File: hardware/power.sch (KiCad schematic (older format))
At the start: 14 parts, among them P201 CONN_02X05, U201 MP1469

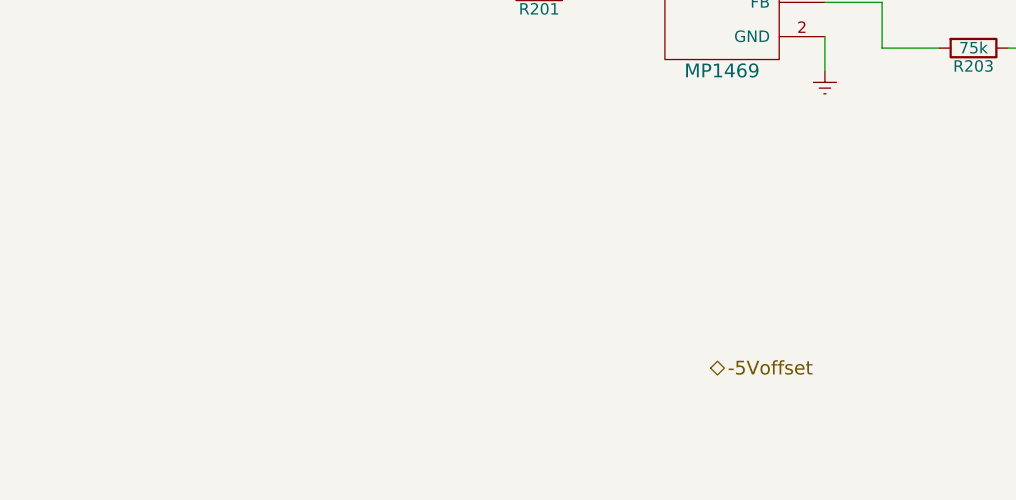
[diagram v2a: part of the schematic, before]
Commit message: updated footprint & first tracks laid
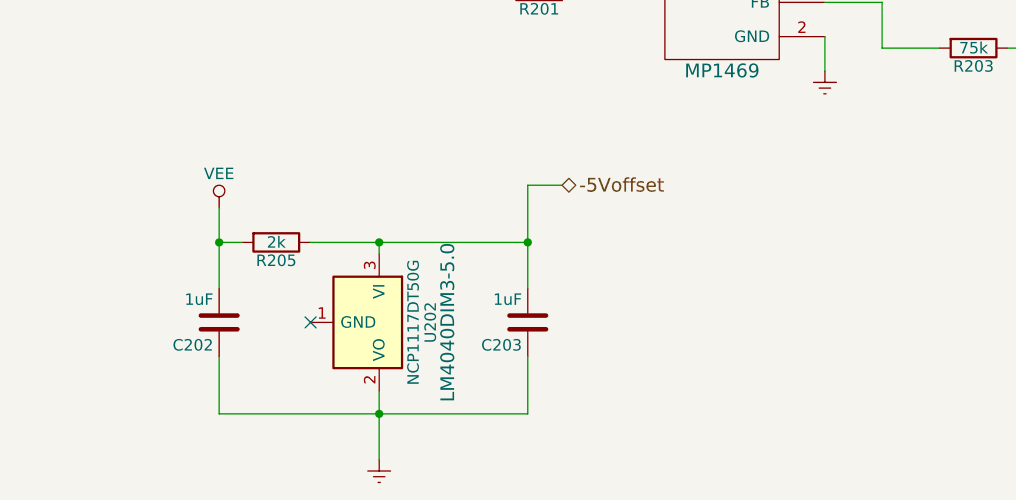
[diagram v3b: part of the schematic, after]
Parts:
- added C202, C203: 1uF, Capacitors_SMD:C_0805_HandSoldering, symbol C
- added R205: 2k, Resistors_SMD:R_0805_HandSoldering, symbol R
- added U202: NCP1117DT50G, TO_SOT_Packages_SMD:SOT-23, symbol NCP1117DT50G
- C201: footprint Capacitors_THT:C_Rect_L11.5mm_W2.8mm_P10.00mm_MKT -> Capacitors_SMD:C_0805_HandSoldering
- C244: footprint Capacitors_THT:C_Axial_L5.1mm_D3.1mm_P7.50mm_Horizontal -> Capacitors_SMD:C_0805_HandSoldering
- CP201, CP202, CP203: footprint Capacitors_THT:CP_Radial_D10.0mm_P5.00mm -> Capacitors_THT:CP_Radial_D5.0mm_P2.00mm
- R201, R202, R203, R204: footprint Resistors_Universal:Resistor_SMD+THTuniversal_0805to1206_RM10_HandSoldering_RevA_Date25Jun2010 -> Resistors_SMD:R_0805_HandSoldering
- U201: footprint (none) -> TO_SOT_Packages_SMD:SOT-23-6
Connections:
- net -5Voffset: now also C203.2, R205.1, U202.3 (VI)
- net Earth: now also C202.1, C203.1, U202.2 (VO)
- net VEE: now also C202.2, R205.2
- no-connect marks 0 -> 1
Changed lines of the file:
@@
 F 0 "CP201" H 4975 2350 50  0000 L CNN
 F 1 "22uF" H 4975 2150 50  0000 L CNN
-F 2 "Capacitors_THT:CP_Radial_D10.0mm_P5.00mm" H 4988 2100 50  0001 C CNN
+F 2 "Capacitors_THT:CP_Radial_D5.0mm_P2.00mm" H 4988 2100 50  0001 C CNN
 F 3 "" H 4950 2250 50  0000 C CNN
 	1    4950 2250
@@
 F 0 "CP202" H 4975 2850 50  0000 L CNN
 F 1 "22uF" H 4975 2650 50  0000 L CNN
-F 2 "Capacitors_THT:CP_Radial_D10.0mm_P5.00mm" H 4988 2600 50  0001 C CNN
+F 2 "Capacitors_THT:CP_Radial_D5.0mm_P2.00mm" H 4988 2600 50  0001 C CNN
 F 3 "" H 4950 2750 50  0000 C CNN
 	1    4950 2750
@@
 F 0 "R201" V 5530 3250 50  0000 C CNN
 F 1 "100k" V 5450 3250 50  0000 C CNN
-F 2 "Resistors_Universal:Resistor_SMD+THTuniversal_0805to1206_RM10_HandSoldering_RevA_Date25Jun2010" V 5380 3250 50  0001 C CNN
+F 2 "Resistors_SMD:R_0805_HandSoldering" V 5380 3250 50  0001 C CNN
 F 3 "" H 5450 3250 50  0000 C CNN
 	1    5450 3250
@@
 F 0 "U201" H 6250 3650 60  0000 C CNN
 F 1 "MP1469" H 6250 2900 60  0000 C CNN
-F 2 "" H 6100 3150 60  0001 C CNN
+F 2 "TO_SOT_Packages_SMD:SOT-23-6" H 6100 3150 60  0001 C CNN
 F 3 "" H 6100 3150 60  0001 C CNN
 	1    6250 3250
@@
 F 0 "C201" V 6900 3050 50  0000 L CNN
 F 1 "1uF" V 7000 3050 50  0000 L CNN
-F 2 "Capacitors_THT:C_Rect_L11.5mm_W2.8mm_P10.00mm_MKT" H 6988 2850 50  0001 C CNN
+F 2 "Capacitors_SMD:C_0805_HandSoldering" H 6988 2850 50  0001 C CNN
 F 3 "" H 6950 3000 50  0000 C CNN
 	1    6950 3000
@@
 F 0 "R203" V 7430 3500 50  0000 C CNN
 F 1 "75k" V 7350 3500 50  0000 C CNN
-F 2 "Resistors_Universal:Resistor_SMD+THTuniversal_0805to1206_RM10_HandSoldering_RevA_Date25Jun2010" V 7280 3500 50  0001 C CNN
+F 2 "Resistors_SMD:R_0805_HandSoldering" V 7280 3500 50  0001 C CNN
 F 3 "" H 7350 3500 50  0000 C CNN
 	1    7350 3500
@@
 F 0 "CP203" H 8225 3400 50  0000 L CNN
 F 1 "22uF" H 8225 3200 50  0000 L CNN
-F 2 "Capacitors_THT:CP_Radial_D10.0mm_P5.00mm" H 8238 3150 50  0001 C CNN
+F 2 "Capacitors_THT:CP_Radial_D5.0mm_P2.00mm" H 8238 3150 50  0001 C CNN
 F 3 "" H 8200 3300 50  0000 C CNN
 	1    8200 3300
@@
 F 0 "R204" V 7880 3700 50  0000 C CNN
 F 1 "7k68" V 7800 3700 50  0000 C CNN
-F 2 "Resistors_Universal:Resistor_SMD+THTuniversal_0805to1206_RM10_HandSoldering_RevA_Date25Jun2010" V 7730 3700 50  0001 C CNN
+F 2 "Resistors_SMD:R_0805_HandSoldering" V 7730 3700 50  0001 C CNN
 F 3 "" H 7800 3700 50  0000 C CNN
 	1    7800 3700
@@
 F 0 "R202" V 7880 3300 50  0000 C CNN
 F 1 "402k2" V 7800 3300 50  0000 C CNN
-F 2 "Resistors_Universal:Resistor_SMD+THTuniversal_0805to1206_RM10_HandSoldering_RevA_Date25Jun2010" V 7730 3300 50  0001 C CNN
+F 2 "Resistors_SMD:R_0805_HandSoldering" V 7730 3300 50  0001 C CNN
 F 3 "" H 7800 3300 50  0000 C CNN
 	1    7800 3300
@@
 F 0 "C244" H 8625 3400 50  0000 L CNN
 F 1 "100nF" H 8625 3200 50  0000 L CNN
-F 2 "Capacitors_THT:C_Axial_L5.1mm_D3.1mm_P7.50mm_Horizontal" H 8638 3150 50  0001 C CNN
+F 2 "Capacitors_SMD:C_0805_HandSoldering" H 8638 3150 50  0001 C CNN
 F 3 "" H 8600 3300 50  0000 C CNN
 	1    8600 3300
@@
 Wire Wire Line
 	6650 1100 6650 1300
-Text HLabel 6200 4900 2    60   BiDi ~ 0
+Text HLabel 5550 4100 2    60   BiDi ~ 0
 -5Voffset
 $Comp
@@
 Wire Wire Line
 	7600 1300 7600 1100
+$Comp
+L NCP1117DT50G U202
+U 1 1 5BE9A6E8
+P 4750 4700
+F 0 "U202" H 4750 4925 50  0000 C CNN
+F 1 "NCP1117DT50G" H 4750 4850 50  0000 C CNN
+F 2 "TO_SOT_Packages_SMD:SOT-23" H 4800 4450 50  0001 L CNN
+F 3 "" H 4750 4700 50  0000 C CNN
+F 4 "LM4040DIM3-5.0" H 4750 5000 60  0000 C CNN "Part Number"
+	1    4750 4700
+	0    1    1    0
+$EndComp
+$Comp
+L VEE #PWR025
+U 1 1 5BE9AB77
+P 4050 4200
+F 0 "#PWR025" H 4050 4050 50  0001 C CNN
+F 1 "VEE" H 4050 4350 50  0000 C CNN
+F 2 "" H 4050 4200 50  0000 C CNN
+F 3 "" H 4050 4200 50  0000 C CNN
+	1    4050 4200
+	1    0    0    -1
+$EndComp
+$Comp
+L C C202
+U 1 1 5BE9ABC7
+P 4050 4700
+F 0 "C202" H 4075 4800 50  0000 L CNN
+F 1 "1uF" H 4075 4600 50  0000 L CNN
+F 2 "Capacitors_SMD:C_0805_HandSoldering" H 4088 4550 50  0001 C CNN
+F 3 "" H 4050 4700 50  0000 C CNN
+	1    4050 4700
+	-1   0    0    1
+$EndComp
+$Comp
+L C C203
+U 1 1 5BE9AF4F
+P 5400 4700
+F 0 "C203" H 5425 4800 50  0000 L CNN
+F 1 "1uF" H 5425 4600 50  0000 L CNN
+F 2 "Capacitors_SMD:C_0805_HandSoldering" H 5438 4550 50  0001 C CNN
+F 3 "" H 5400 4700 50  0000 C CNN
+	1    5400 4700
+	-1   0    0    1
+$EndComp
+$Comp
+L Earth #PWR026
+U 1 1 5BE9B08F
+P 4750 5300
+F 0 "#PWR026" H 4750 5050 50  0001 C CNN
+F 1 "Earth" H 4750 5150 50  0001 C CNN
+F 2 "" H 4750 5300 50  0000 C CNN
+F 3 "" H 4750 5300 50  0000 C CNN
+	1    4750 5300
+	1    0    0    -1
+$EndComp
+Wire Wire Line
+	4750 5000 4750 5300
+Wire Wire Line
+	5400 5100 5400 4850
+Wire Wire Line
+	4050 5100 5400 5100
+Connection ~ 4750 5100
+Wire Wire Line
+	4050 4850 4050 5100
+$Comp
+L R R205
+U 1 1 5BE9B1DC
+P 4300 4350
+F 0 "R205" V 4380 4350 50  0000 C CNN
+F 1 "2k" V 4300 4350 50  0000 C CNN
+F 2 "Resistors_SMD:R_0805_HandSoldering" V 4230 4350 50  0001 C CNN
+F 3 "" H 4300 4350 50  0000 C CNN
+	1    4300 4350
+	0    1    1    0
+$EndComp
+Wire Wire Line
+	4050 4200 4050 4550
+Wire Wire Line
+	4050 4350 4150 4350
+Connection ~ 4050 4350
+Wire Wire Line
+	4450 4350 5400 4350
+Wire Wire Line
+	4750 4350 4750 4400
+Wire Wire Line
+	5400 4100 5400 4550
+Connection ~ 4750 4350
+Wire Wire Line
+	5550 4100 5400 4100
+Connection ~ 5400 4350
+NoConn ~ 4450 4700
 $EndSCHEMATC

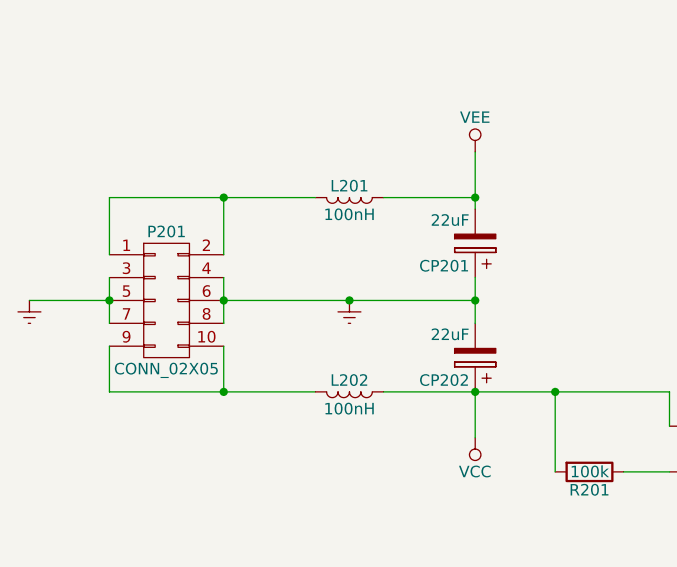
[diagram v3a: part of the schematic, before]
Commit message: finalized most footprints and nets.
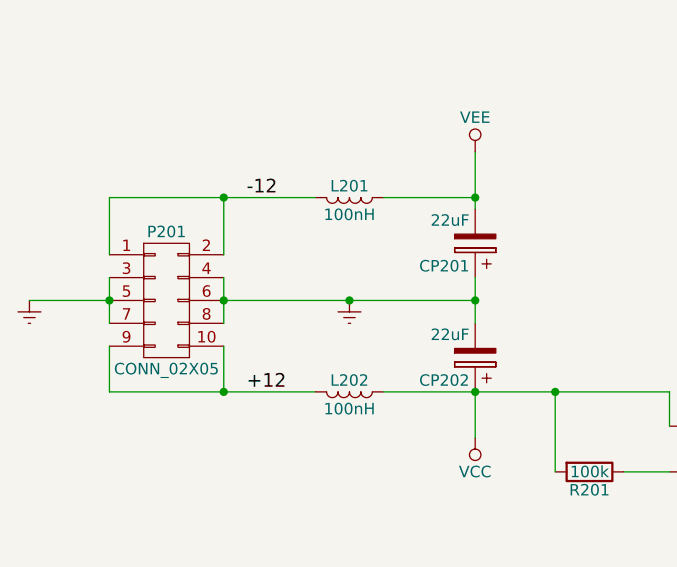
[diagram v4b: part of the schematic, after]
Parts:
- L201, L202: footprint Choke_SMD:Choke_Double_SMD_Wuerth-WE-DD-Typ-M-Typ-S -> Choke_Axial_ThroughHole:Choke_Horizontal_RM10mm
- L203: footprint Choke_Toroid_ThroughHole:Choke_Toroid_horizontal_Diameter4-5mm_Amidon-T16 -> Choke_Axial_ThroughHole:Choke_Horizontal_RM10mm
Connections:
- net -12: now reaches L201.2, P201.1 (P1), P201.2 (P2)
- net +12: now reaches L202.2, P201.10 (P10), P201.9 (P9)
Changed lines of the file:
@@
 F 0 "L201" V 4350 2050 50  0000 C CNN
 F 1 "100nH" V 4475 2050 50  0000 C CNN
-F 2 "Choke_SMD:Choke_Double_SMD_Wuerth-WE-DD-Typ-M-Typ-S" H 4400 2050 50  0001 C CNN
+F 2 "Choke_Axial_ThroughHole:Choke_Horizontal_RM10mm" H 4400 2050 50  0001 C CNN
 F 3 "" H 4400 2050 50  0000 C CNN
 	1    4400 2050
@@
 F 0 "L202" V 4350 2900 50  0000 C CNN
 F 1 "100nH" V 4475 2900 50  0000 C CNN
-F 2 "Choke_SMD:Choke_Double_SMD_Wuerth-WE-DD-Typ-M-Typ-S" H 4400 2900 50  0001 C CNN
+F 2 "Choke_Axial_ThroughHole:Choke_Horizontal_RM10mm" H 4400 2900 50  0001 C CNN
 F 3 "" H 4400 2900 50  0000 C CNN
 	1    4400 2900
@@
 F 0 "L203" V 7450 3150 50  0000 C CNN
 F 1 "6u8H" V 7575 3150 50  0000 C CNN
-F 2 "Choke_Toroid_ThroughHole:Choke_Toroid_horizontal_Diameter4-5mm_Amidon-T16" H 7500 3150 50  0001 C CNN
+F 2 "Choke_Axial_ThroughHole:Choke_Horizontal_RM10mm" H 7500 3150 50  0001 C CNN
 F 3 "" H 7500 3150 50  0000 C CNN
 	1    7500 3150
@@
 Connection ~ 5400 4350
 NoConn ~ 4450 4700
+Text Label 3950 2900 0    60   ~ 0
++12
+Text Label 3950 2050 0    60   ~ 0
+-12
 $EndSCHEMATC

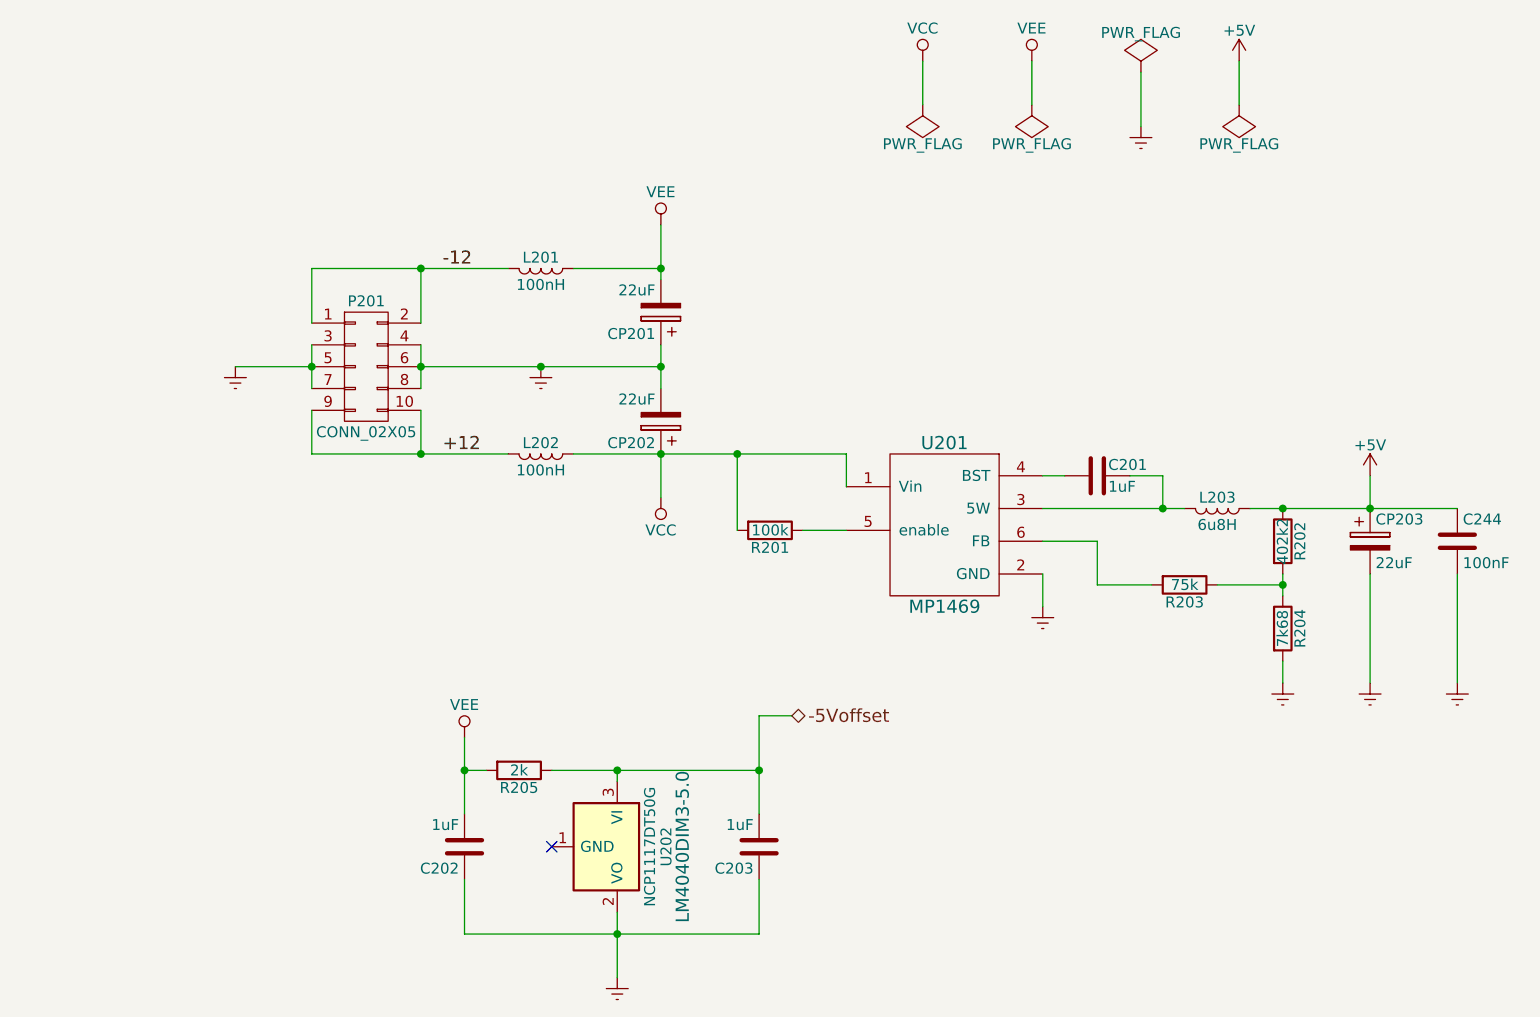
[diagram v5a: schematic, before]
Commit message: removal of +12 to +5 stepdown since i've got no CV outputs.
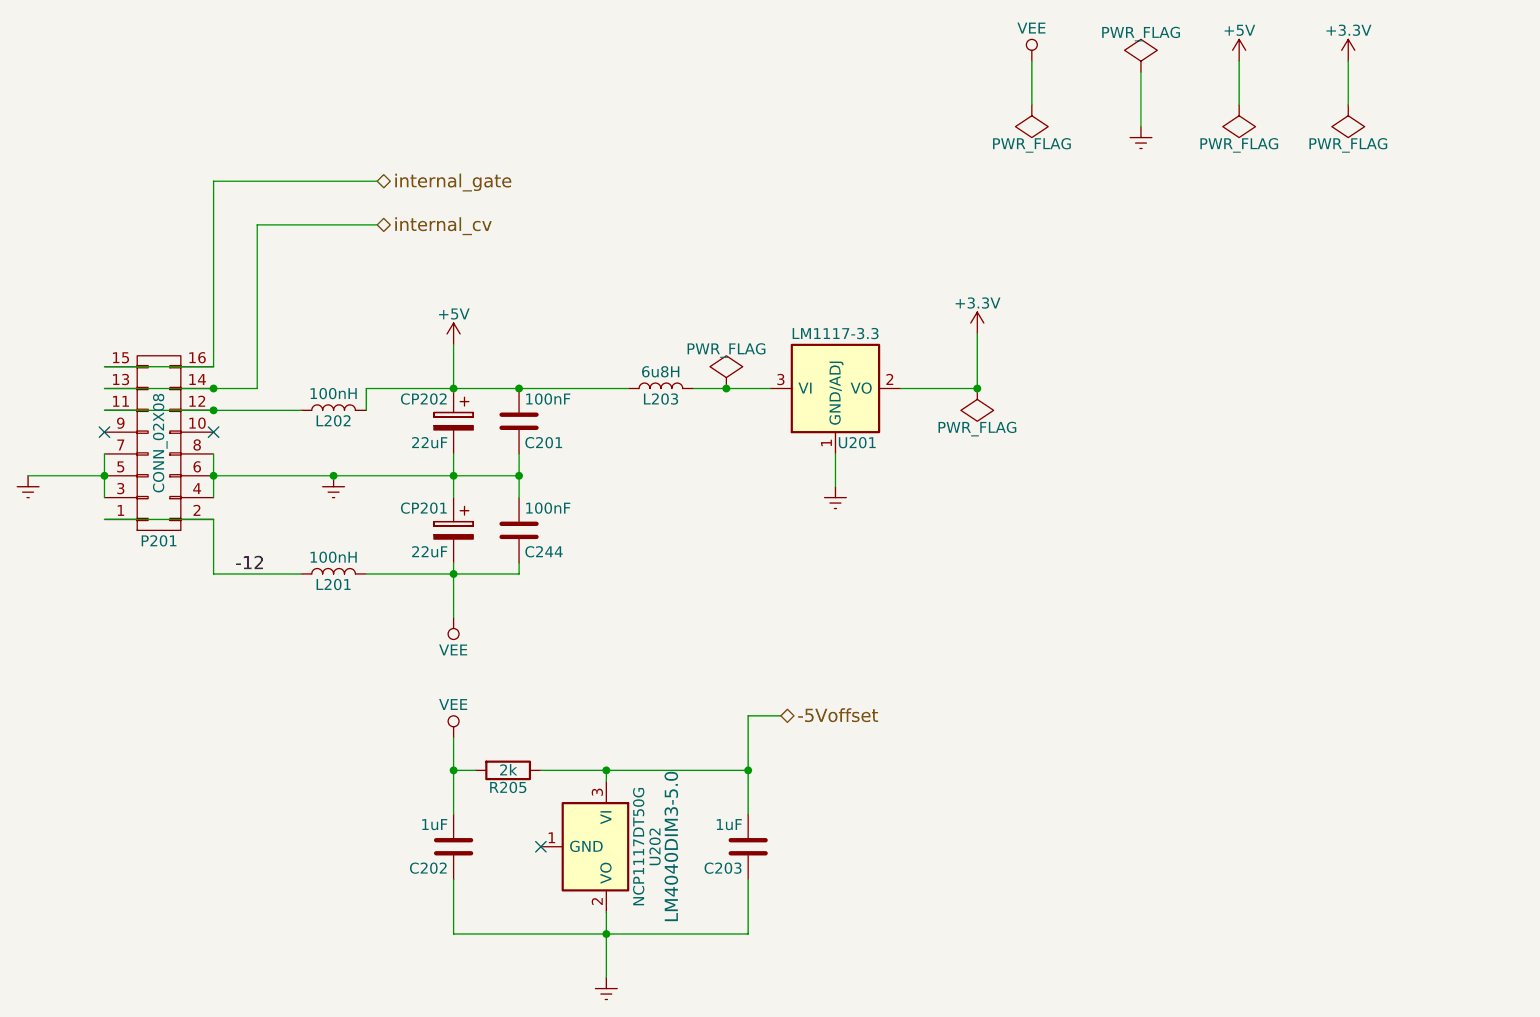
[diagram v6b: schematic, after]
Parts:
- removed CP203: 22uF, Capacitors_THT:CP_Radial_D5.0mm_P2.00mm, symbol CP
- removed P201: CONN_02X05, Connectors:IDC_Header_Straight_10pins, symbol CONN_02X05
- removed R201: 100k, Resistors_SMD:R_0805_HandSoldering, symbol R
- removed R202: 402k2, Resistors_SMD:R_0805_HandSoldering, symbol R
- removed R203: 75k, Resistors_SMD:R_0805_HandSoldering, symbol R
- removed R204: 7k68, Resistors_SMD:R_0805_HandSoldering, symbol R
- removed U201: MP1469, TO_SOT_Packages_SMD:SOT-23-6, symbol MP1469
- added P201: CONN_02X08, symbol CONN_02X08
- added U201: LM1117-3.3, symbol LM1117-3.3
- C201: value 1uF -> 100nF
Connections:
- net VCC is gone; now on net +5V: CP202.1, L202.1
- net +5V: now also C201.2, L203.2; no longer C244.1, L203.1
- net -12: now also P201.1 (P1), P201.2 (P2)
- net Earth: now also C201.1, P201.3 (P3), P201.4 (P4), P201.5 (P5), P201.6 (P6), P201.7 (P7), P201.8 (P8), U201.1 (GND/ADJ)
- net VEE: now also C244.1
- net +12: no longer names the net of L202.2
- net +12: now also P201.11 (P11), P201.12 (P12)
- new net: L203.1, U201.3 (VI)
- new net +3V3: U201.2 (VO), U201.4 (VO)
- new net internal_cv: P201.13 (P13), P201.14 (P14)
- new net internal_gate: P201.15 (P15), P201.16 (P16)
- no-connect marks 1 -> 3
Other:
- moved on the sheet: C202, C203, C244, CP201, CP202, L201, L203, R205, U202
